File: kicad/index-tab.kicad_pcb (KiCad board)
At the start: 2 copper layers, 254 x 140 mm, 202 parts, among them J1 USB_C_Receptacle_USB2.0, SW1 SW_Push, U1 ATmega32U4-AU, Y1 16MHz

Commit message: finished adding stabs
There is no way to many possiblities at the bottom row
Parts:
- removed the REF** at (152.4, 152.4)
- added REF**: MountingHole_2.2mm_M2, MountingHole:MountingHole_2.2mm_M2, F.Cu at (256.9, 44.5)
- added REF**: 3U, index-tab:MXOnly-3U-NoLED, F.Cu at (171.4, 152.4)
- added REF**: 3U, index-tab:MXOnly-3U-NoLED, F.Cu at (190.5, 152.4)
- added REF**: 3U, index-tab:MXOnly-3U-NoLED, F.Cu at (133.3, 152.4)
- added REF**: 3U, index-tab:MXOnly-3U-NoLED, F.Cu at (114.3, 152.4)
- added REF**: Stabilizer_MX_2u, index-tab:Stabilizer_MX_2u, F.Cu at (200.0, 152.4)
- added REF**: Stabilizer_MX_2u, index-tab:Stabilizer_MX_2u, F.Cu at (181.0, 152.4)
- added REF**: Stabilizer_MX_2u, index-tab:Stabilizer_MX_2u, F.Cu at (161.9, 152.4)
- added REF**: Stabilizer_MX_2u, index-tab:Stabilizer_MX_2u, F.Cu at (142.9, 152.4)
- added REF**: Stabilizer_MX_2u, index-tab:Stabilizer_MX_2u, F.Cu at (123.8, 152.4)
- added REF**: Stabilizer_MX_2u, index-tab:Stabilizer_MX_2u, F.Cu at (104.8, 152.4)
- added REF**: MountingHole_2.2mm_M2, MountingHole:MountingHole_2.2mm_M2, F.Cu at (256.9, 142.9)
- added REF**: MountingHole_2.2mm_M2, MountingHole:MountingHole_2.2mm_M2, F.Cu at (256.9, 104.7)
- added REF**: MountingHole_2.2mm_M2, MountingHole:MountingHole_2.2mm_M2, F.Cu at (161.8, 142.9)
- added REF**: MountingHole_2.2mm_M2, MountingHole:MountingHole_2.2mm_M2, F.Cu at (161.8, 66.8)
- added REF**: MountingHole_2.2mm_M2, MountingHole:MountingHole_2.2mm_M2, F.Cu at (142.5, 104.7)
- added REF**: MountingHole_2.2mm_M2, MountingHole:MountingHole_2.2mm_M2, F.Cu at (47.6, 142.9)
- added REF**: MountingHole_2.2mm_M2, MountingHole:MountingHole_2.2mm_M2, F.Cu at (47.6, 104.7)
- added REF**: MountingHole_2.2mm_M2, MountingHole:MountingHole_2.2mm_M2, F.Cu at (47.6, 66.8)
- moved CR7 27.0 mm to (75.9, 159.2), turned to 90 degrees
- moved RGB7 26.2 mm to (81.8, 159.8)
- moved CR8 22.5 mm to (218.8, 155.3)
- moved RGB8 21.7 mm to (220.8, 159.8)
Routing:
- net ROW5: track 229.6 -> 386.9 mm
- net Net-(RGB7-Pad2): track 0.00 -> 149.6 mm
- net /+5v: track 928.3 -> 1025.2 mm
- net Net-(RGB8-Pad2): track 0.00 -> 70.2 mm
- net Net-(RGB6-Pad2): track 20.3 -> 81.2 mm
- net Net-(D78-Pad2): track 0.00 -> 42.8 mm, vias 0 -> 2
- net Net-(D30-Pad2): track 0.30 -> 43.1 mm, vias 0 -> 2
- net Net-(D52-Pad2): track 0.30 -> 43.1 mm, vias 0 -> 2
- net Net-(D77-Pad2): track 0.00 -> 42.5 mm, vias 0 -> 2
- net Net-(D41-Pad2): track 6.18 -> 43.8 mm, vias 0 -> 2
- net Net-(D24-Pad2): track 6.18 -> 33.3 mm
- net COL6: track 196.4 -> 215.8 mm, vias 7 -> 8
- net COL8: track 158.2 -> 174.6 mm, vias 7 -> 8
- net COL3: track 253.3 -> 269.7 mm, vias 7 -> 8
- net COL5: track 216.5 -> 232.8 mm, vias 7 -> 8
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
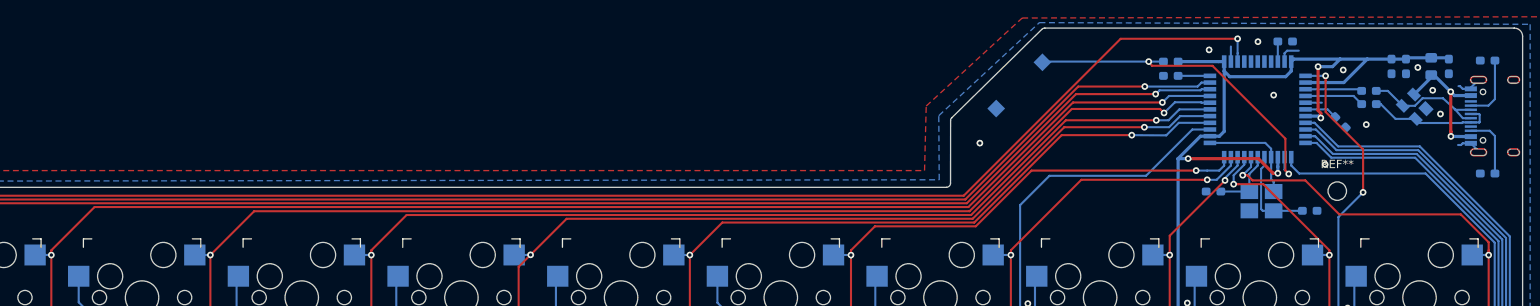
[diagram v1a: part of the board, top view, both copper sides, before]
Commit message: OLED screen added
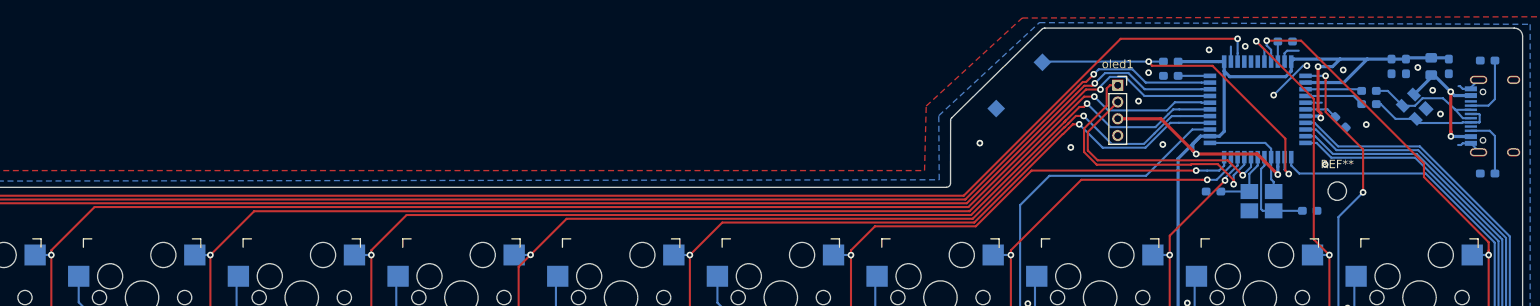
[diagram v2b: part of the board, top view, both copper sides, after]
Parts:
- added oled1: Conn_01x04_Female, Connector_PinSocket_2.00mm:PinSocket_1x04_P2.00mm_Vertical, F.Cu at (230.7, 31.8)
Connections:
- U1 pad 18: COL12 -> /SCK
- U1 pad 19: COL11 -> /SDA
- U1 pad 40: Net-(U1-Pad40) -> COL11
- U1 pad 41: Net-(U1-Pad41) -> COL12
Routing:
- net /SDA: track 0.00 -> 33.7 mm, vias 0 -> 1
- net /SCK: track 0.00 -> 29.6 mm, vias 0 -> 1
- net COL11: track 128.6 -> 141.6 mm
- net /+5v: track 1025.2 -> 1037.1 mm
- net GND: track 25.5 -> 30.9 mm, vias 42 -> 47
- net COL12: track 144.4 -> 149.2 mm
- net COL6: track 215.8 -> 218.5 mm
- net COL5: track 232.8 -> 235.4 mm
- net COL7: track 191.7 -> 194.0 mm
- net COL3: track 269.7 -> 271.8 mm
- net COL2: track 272.6 -> 274.2 mm
- net COL1: track 291.7 -> 293.0 mm
- net COL4: track 250.0 -> 250.9 mm

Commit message: Changed the mountin hole
Can now have a seperate plate for the oled/top. Also added the monster head back in
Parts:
- removed the REF** at (256.9, 44.5)
- added G***: LOGO, index-tab:monster, F.Cu at (221.2, 111.5)
- added REF**: MountingHole_2.2mm_M2, MountingHole:MountingHole_2.2mm_M2, F.Cu at (263.1, 41.5)
- added REF**: MountingHole_2.2mm_M2, MountingHole:MountingHole_2.2mm_M2, F.Cu at (214.0, 38.0)
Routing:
- net RGB: track 54.9 -> 52.4 mm
- net ROW2: track 307.7 -> 308.5 mm
- net GND: vias 47 -> 49
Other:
- board text added: "by kyrremann.no | rev4"
- board text removed: "by kyrremann.no | rev3"

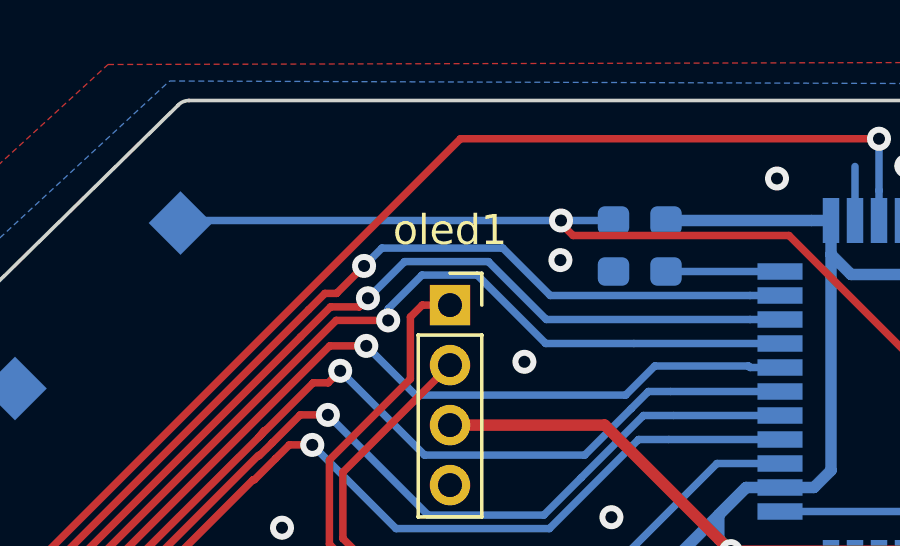
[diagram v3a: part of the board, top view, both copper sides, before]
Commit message: rev4: I think
This is so old I'm not really sure what it is. Going to make rev5 anyway, so just ignore this.
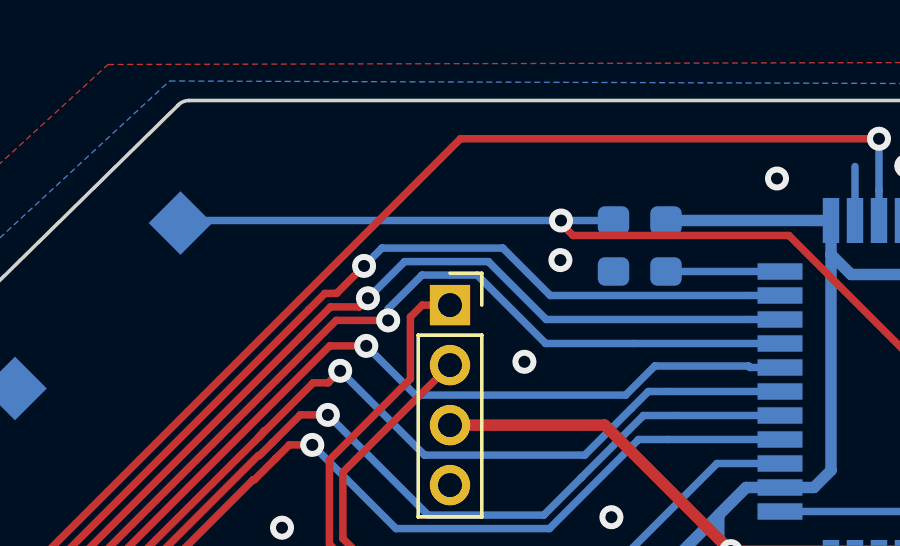
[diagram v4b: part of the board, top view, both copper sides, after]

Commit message: rev5: updated schematic
This is heavily inspired by Plain60 by evyd13
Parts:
- removed C7, CR1, CR10, CR2, CR3, CR4, CR5, CR6, CR7, CR8, CR9: 0.1uF, Capacitor_SMD:C_0603_1608Metric_Pad1.05x0.95mm_HandSolder
- removed D101: PRTR5V0U2X, Package_TO_SOT_SMD:SOT-143
- removed G***: LOGO, index-tab:monster
- removed REF** (x10): MountingHole_2.2mm_M2, MountingHole:MountingHole_2.2mm_M2
- removed REF** (x4): 3U, index-tab:MXOnly-3U-NoLED
- removed REF** (x6): Stabilizer_MX_2u, index-tab:Stabilizer_MX_2u
- removed oled1: Conn_01x04_Female, Connector_PinSocket_2.00mm:PinSocket_1x04_P2.00mm_Vertical
- added J2: Conn_01x04_Female, index-tab:JST_SH_SM04B-SRSS-TB_1x04-1MP_P1.00mm_Horizontal, B.Cu at (267.9, 15.3)
- added U2: USBLC6-2SC6, Package_TO_SOT_SMD:SOT-23-6, B.Cu at (260.3, 9.17)
- C1, C2: value 22pF -> 0.1uF; footprint Capacitor_SMD:C_0603_1608Metric_Pad1.05x0.95mm_HandSolder -> Capacitor_SMD:C_0603_1608Metric
- C3, C4: value 1uF -> 0.1uF; footprint Capacitor_SMD:C_0603_1608Metric_Pad1.05x0.95mm_HandSolder -> Capacitor_SMD:C_0603_1608Metric
- C5: value 0.1uF -> 4.7uF; footprint Capacitor_SMD:C_0603_1608Metric_Pad1.05x0.95mm_HandSolder -> Capacitor_SMD:C_0603_1608Metric
- C6: footprint Capacitor_SMD:C_0603_1608Metric_Pad1.05x0.95mm_HandSolder -> Capacitor_SMD:C_0603_1608Metric
- F1: value 6v 0.5A -> Polyfuse; footprint Fuse:Fuse_0805_2012Metric_Pad1.15x1.40mm_HandSolder -> Fuse:Fuse_0603_1608Metric
- R1, R2, R3, R4, R5, R6: footprint Resistor_SMD:R_0603_1608Metric_Pad1.05x0.95mm_HandSolder -> Resistor_SMD:R_0603_1608Metric
- SW1: footprint Button_Switch_SMD:SW_SPST_CK_RS282G05A3 -> Button_Switch_SMD:SW_DIP_SPSTx01_Slide_6.7x4.1mm_W6.73mm_P2.54mm_LowProfile_JPin
- Y1: value 16MHz -> Resonator; footprint Crystal:Crystal_SMD_3225-4Pin_3.2x2.5mm_HandSoldering -> Crystal:Resonator_SMD_muRata_CSTxExxV-3Pin_3.0x1.1mm_HandSoldering
- moved SW1 42.3 mm to (258.2, 16.2), turned to 0 degrees
- moved C2 41.8 mm to (274.3, 17.9)
- moved C1 39.6 mm to (255.0, 7.25)
- moved R5 38.2 mm to (268.8, 7.73)
- moved Y1 35.6 mm to (255.6, 10.9), turned to 0 degrees
- moved C6 29.5 mm to (264.8, 7.73), turned to 0 degrees
- moved C3 20.1 mm to (264.8, 10.2), turned to 0 degrees
- moved C5 19.7 mm to (268.8, 10.2), turned to 0 degrees
- moved C4 18.0 mm to (274.3, 15.3), turned to 0 degrees
- moved F1 17.9 mm to (274.3, 12.8), turned to 0 degrees
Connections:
- net /V_BUS renamed /VBUS
- C1 pad 1: /XTAL2 -> VCC
- C2 pad 1: GND -> VCC
- C2 pad 2: /XTAL1 -> GND
- C3 pad 1: /+5v -> VCC
- C4 pad 1: /+5v -> VCC
- C5 pad 1: /+5v -> VCC
- C6 pad 1: /UCAP -> GND
- C6 pad 2: GND -> Net-(C6-Pad2)
- F1 pad 1: /+5v -> VCC
- R5 pad 1: /RESET -> VCC
- R5 pad 2: /+5v -> /RESET
- U1 pad 14: /+5v -> VCC
- U1 pad 18: /SCK -> Net-(U1-Pad18)
- U1 pad 19: /SDA -> Net-(U1-Pad19)
- U1 pad 2: /+5v -> VCC
- U1 pad 24: /+5v -> VCC
- U1 pad 34: /+5v -> VCC
- U1 pad 42: /AREF -> Net-(U1-Pad42)
- U1 pad 44: /+5v -> VCC
- U1 pad 6: /UCAP -> Net-(C6-Pad2)
- U1 pad 7: /+5v -> VCC
- Y1 pad 1: /XTAL2 -> /XTAL1
- Y1 pad 3: /XTAL1 -> /XTAL2
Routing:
- net Net-(U1-Pad19): track 0.00 -> 33.7 mm, vias 0 -> 1
- net /SDA: track 33.7 -> 0.00 mm, vias 1 -> 0
- net Net-(U1-Pad18): track 0.00 -> 29.6 mm, vias 0 -> 1
- net /SCK: track 29.6 -> 0.00 mm, vias 1 -> 0
- net Net-(C6-Pad2): track 0.00 -> 3.93 mm
- net /UCAP: track 3.93 -> 0.00 mm
- net Net-(U1-Pad42): track 0.00 -> 2.40 mm
- net /AREF: track 2.40 -> 0.00 mm

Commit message: rev5: MCU schematic and pcb should be done
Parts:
- moved SW1 43.1 mm to (218.2, 32.3), turned to 45 degrees
- moved R5 42.0 mm to (251.5, 46.0), turned to 90 degrees
- moved C3 40.2 mm to (249.8, 47.6), turned to 270 degrees
- moved Y1 36.2 mm to (245.7, 45.7)
- moved C1 35.5 mm to (237.0, 37.9), turned to 180 degrees
- moved C2 32.9 mm to (242.6, 26.7), turned to 180 degrees
- moved C6 28.2 mm to (256.4, 34.7), turned to 180 degrees
- moved U2 27.2 mm to (267.2, 35.5), turned to 180 degrees
- moved C4 24.9 mm to (252.2, 26.7)
- moved C5 23.5 mm to (257.2, 30.7), turned to 90 degrees
- moved F1 22.0 mm to (262.9, 31.7), turned to 270 degrees
- moved J2 13.1 mm to (267.6, 28.4)
- moved R3 3.26 mm to (262.9, 36.5)
- moved R4 3.03 mm to (262.9, 34.5)
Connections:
- J1 pad A6: /D+ -> /USB_D+
- J1 pad A7: /D- -> /USB_D-
- J1 pad B6: /D+ -> /USB_D+
- J1 pad B7: /D- -> /USB_D-
- J2 pad 2: /D- -> /USB_D-
- J2 pad 3: /D+ -> /USB_D+
- RGB1 pad 1: /+5v -> VCC
- RGB10 pad 1: /+5v -> VCC
- RGB2 pad 1: /+5v -> VCC
- RGB3 pad 1: /+5v -> VCC
- RGB4 pad 1: /+5v -> VCC
- RGB5 pad 1: /+5v -> VCC
- RGB6 pad 1: /+5v -> VCC
- RGB7 pad 1: /+5v -> VCC
- RGB8 pad 1: /+5v -> VCC
- RGB9 pad 1: /+5v -> VCC
- U1 pad 21: COL9 -> ROW0
- U1 pad 22: COL8 -> COL9
- U1 pad 25: ROW0 -> COL8
- U2 pad 1: /D- -> /USB_D-
- U2 pad 3: /D+ -> /USB_D+
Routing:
- net /+5v: track 1037.1 -> 0.00 mm, vias 8 -> 0
- net VCC: track 0.00 -> 1022.8 mm, vias 0 -> 6
- net Net-(U1-Pad19): track 33.7 -> 0.00 mm, vias 1 -> 0
- net Net-(U1-Pad18): track 29.6 -> 0.00 mm, vias 1 -> 0
- net /USB_D+: track 0.00 -> 17.0 mm, vias 0 -> 2
- net /USB_D-: track 0.00 -> 14.1 mm, vias 0 -> 2
- net /D-: track 15.4 -> 2.41 mm
- net /D+: track 15.3 -> 2.41 mm
- net /VBUS: track 16.7 -> 27.1 mm, vias 2 -> 0
- net /XTAL2: track 11.4 -> 5.84 mm
- net GND: track 30.9 -> 35.6 mm, vias 49 -> 16
- net COL10: track 122.4 -> 126.0 mm, vias 7 -> 6
- net Net-(R3-Pad1): track 7.10 -> 10.4 mm
- net COL12: track 149.2 -> 146.0 mm
- net Net-(R4-Pad1): track 6.77 -> 9.94 mm
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
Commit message: rev5: fixed 2x2u and 7u stabs
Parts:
- removed MX79, MX81, MX83, MX84: MX-NoLED, index-tab:Kailh_socket_MX
- added STAB1: 7u, index-tab:MXOnly-7U-Hotswap, F.Cu at (152.4, 152.4)
- added STAB2: 2u, index-tab:Stabilizer_MX_2u, F.Cu at (123.8, 152.4)
- added STAB3: 2u, index-tab:Stabilizer_MX_2u, F.Cu at (161.9, 152.4)
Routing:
- net Net-(D24-Pad2): track 33.3 -> 6.18 mm
- net VCC: track 1022.8 -> 1000.1 mm
- net COL3: track 269.7 -> 253.3 mm, vias 8 -> 7
- net COL5: track 232.8 -> 216.5 mm, vias 8 -> 7
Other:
- board text added: "by kyrremann.no | rev5"
- board text removed: "by kyrremann.no | rev4"
